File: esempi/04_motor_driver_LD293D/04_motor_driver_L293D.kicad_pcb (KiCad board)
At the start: 2 copper layers, 59.7 x 24.1 mm, 27 parts, among them IC1 L293D, J1 Arduino_Nano_Header, P1 OUT12, P10 SER, P11 EXT_MOT, P2 ALIM_HALL, P3 CONN_MOT1, P4 OUT34, P5 HALL_01, P6 HOLE1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

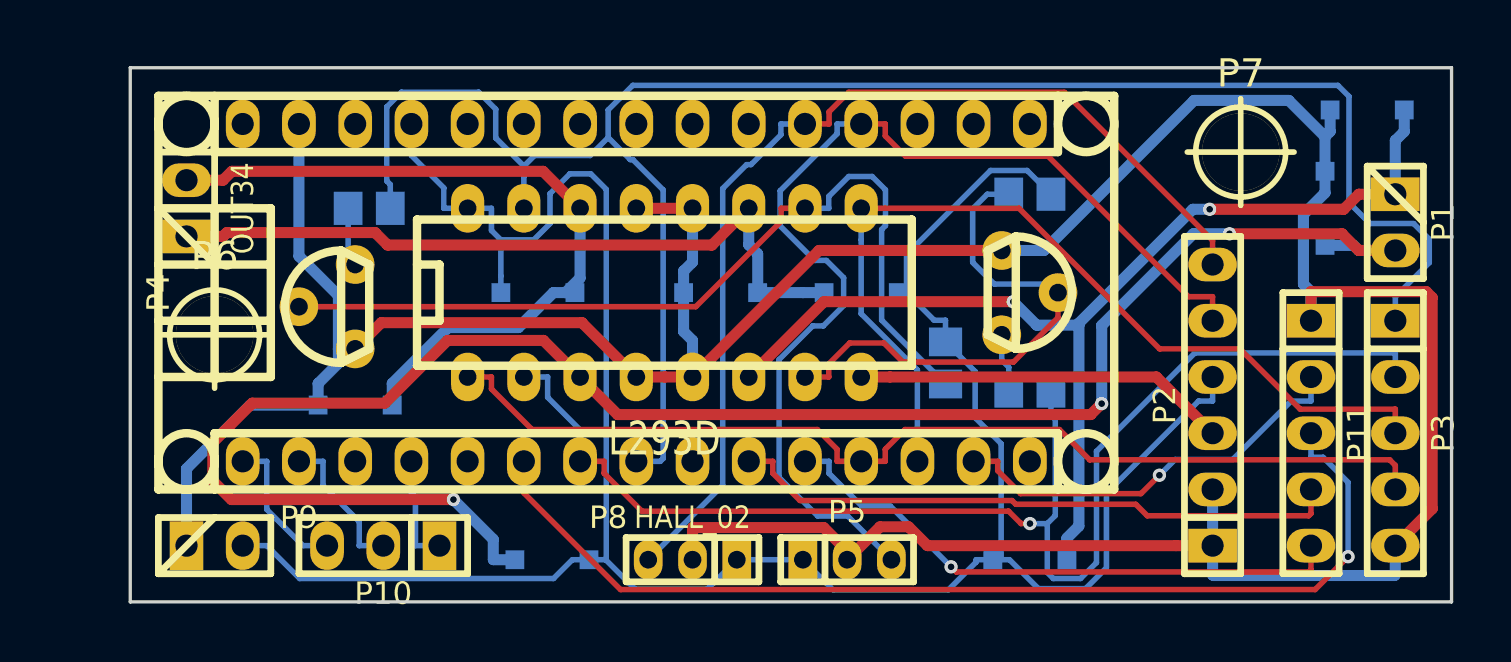
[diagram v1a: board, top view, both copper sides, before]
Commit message: Modifiche a Raspibo gadget e L293D
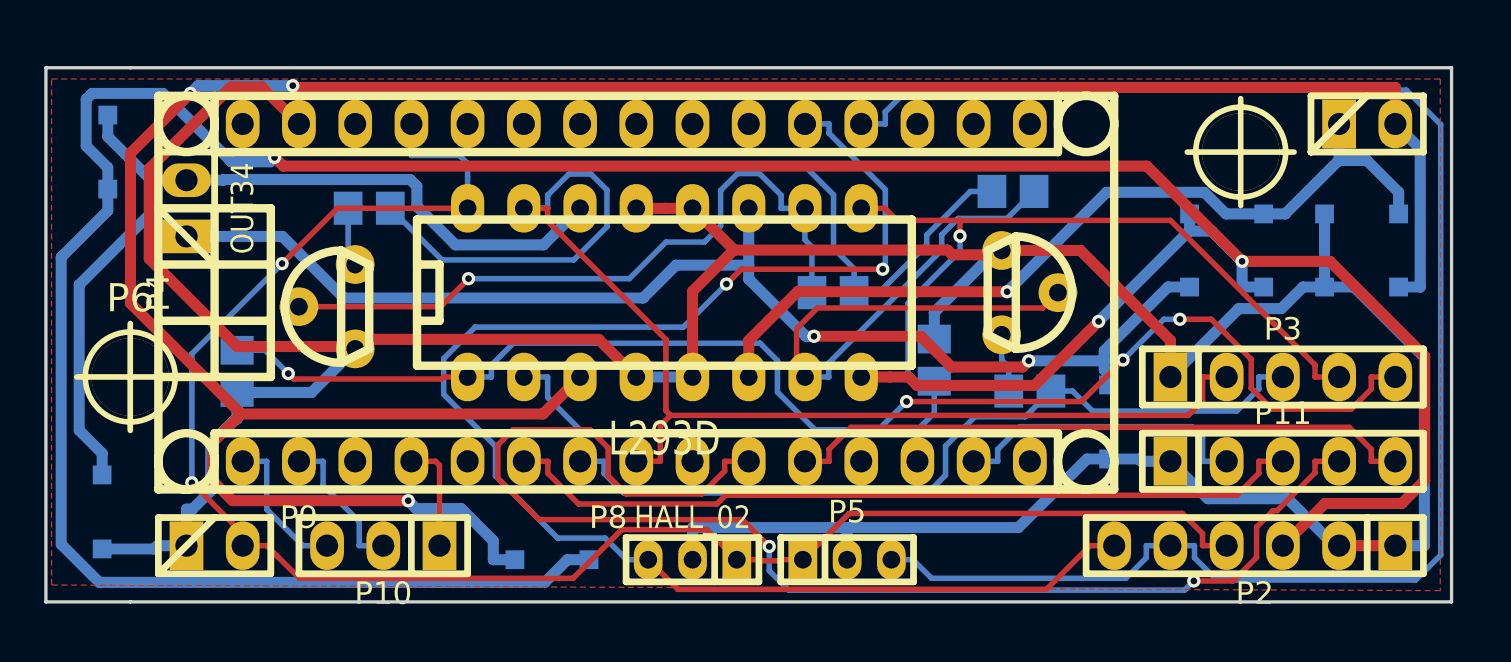
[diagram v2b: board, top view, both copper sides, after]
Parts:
- added R5: R, w_smd_resistors:r_0805, B.Cu at (96.3, 77.2)
- added R6: R, w_smd_resistors:r_0805, B.Cu at (127.8, 76.7)
- moved D5 20.4 mm to (90.4, 67.3), turned to 90 degrees
- moved D8 18.5 mm to (135.6, 79.5), turned to 270 degrees
- moved D1 18.0 mm to (141.0, 70.1)
- moved D7 16.5 mm to (141.0, 73.4)
- moved D6 12.4 mm to (90.2, 83.6), turned to 270 degrees
- moved P2 6.63 mm to (142.2, 85.1), turned to 180 degrees
- moved R3 5.99 mm to (123.2, 73.7), turned to 0 degrees
- moved P3 5.68 mm to (143.5, 77.5), turned to 0 degrees
- moved D2 4.71 mm to (147.1, 70.1)
- moved P1 4.62 mm to (147.3, 66.0), turned to 0 degrees
- moved P6 4.26 mm to (91.4, 77.5)
- moved D4 3.92 mm to (147.1, 73.4), turned to 180 degrees
- moved P11 1.80 mm to (143.5, 81.3), turned to 0 degrees
- moved R2 0.77 mm to (131.3, 69.1), turned to 180 degrees
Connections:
- net Net-(IC1-Pad10) renamed /COLL
- net Net-(IC1-Pad7) renamed /COLL-1
- net Net-(Q1-Pad1) renamed /BASE-1
- net Net-(Q2-Pad1) renamed /BASE-2
- D1 pad 1: +5V -> VCC
- D3 pad 1: +5V -> VCC
- D5 pad 1: +5V -> VCC
- D7 pad 1: +5V -> VCC
- J1 pad 15: (no net) -> Net-(J1-Pad15)
- J1 pad 16: (no net) -> Net-(J1-Pad16)
- J1 pad 17: (no net) -> Net-(J1-Pad17)
- J1 pad 18: (no net) -> Net-(J1-Pad18)
- J1 pad 21: (no net) -> Net-(J1-Pad21)
- J1 pad 22: (no net) -> Net-(J1-Pad22)
- J1 pad 23: (no net) -> Net-(J1-Pad23)
- J1 pad 24: (no net) -> Net-(J1-Pad24)
- J1 pad 25: (no net) -> Net-(J1-Pad25)
- J1 pad 26: (no net) -> Net-(J1-Pad26)
- J1 pad 28: (no net) -> Net-(J1-Pad28)
- J1 pad 3: (no net) -> Net-(J1-Pad3)
- J1 pad 30: (no net) -> Net-(J1-Pad30)
- J1 pad 5: (no net) -> Net-(J1-Pad5)
- J1 pad 9: (no net) -> Net-(J1-Pad9)
- P3 pad 1: 3,4DIR -> GND
- P3 pad 2: 1,2DIR -> 3,4DIR
- P3 pad 3: 3,4EN -> 1,2DIR
- P3 pad 4: 1,2EN -> 3,4EN
- P3 pad 5: GND -> 1,2EN
- P6 pad 1: (no net) -> Net-(P6-Pad1)
- P7 pad 1: (no net) -> Net-(P7-Pad1)
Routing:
- net VCC: track 16.9 -> 149.0 mm, vias 0 -> 3
- net Net-(D3-Pad2): track 83.1 -> 117.9 mm
- net Net-(J1-Pad10): track 27.9 -> 60.2 mm, vias 0 -> 2
- net Net-(J1-Pad19): track 48.2 -> 74.7 mm
- net 3,4DIR: track 85.2 -> 60.6 mm
- net Net-(D7-Pad2): track 33.4 -> 54.9 mm, vias 0 -> 2
- net Net-(J1-Pad20): track 46.6 -> 67.4 mm, vias 0 -> 2
- net 1,2DIR: track 60.6 -> 42.2 mm, vias 1 -> 0
- net 1,2EN: track 46.8 -> 63.2 mm, vias 0 -> 4
- net Net-(J1-Pad6): track 47.7 -> 36.5 mm, vias 1 -> 0
- net Net-(D1-Pad2): track 48.4 -> 38.4 mm, vias 2 -> 1
- net /COLL: track 39.9 -> 31.2 mm, vias 0 -> 1
- net GND: track 155.9 -> 163.8 mm
- net Net-(D5-Pad2): track 33.7 -> 40.7 mm
- net /COLL-1: track 23.5 -> 29.4 mm
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- added copper zone on F.Cu, net GND
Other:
- board size 59.7 x 24.1 mm -> 63.5 x 24.1 mm
